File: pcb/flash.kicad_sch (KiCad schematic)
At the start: 7 parts, among them U4 W25Q128JVS

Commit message: Update project
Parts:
- added R29, R30, R31: 22, symbol Device:R_Small_US
- C23: value 1u -> 100n
- R15, R16, R18: value 22 -> 47k
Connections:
- net +3V3: now also R15.1, R16.1, R18.1
- net IO1: now also R29.1; no longer R15.1
- net IO2: now also R30.1; no longer R16.1
- net IO3: now also R31.1; no longer R18.1
- net ~{CS}: now also R15.2
- net at U4.2 (DO/IO_{1}): now also R16.2, R29.2; no longer R15.2
- net at R18.2: now also U4.3 (~{WP}/IO_{2}), R30.2; no longer U4.7 (~{HOLD}/~{RESET}/IO_{3})
- new net: R31.2, U4.7 (~{HOLD}/~{RESET}/IO_{3})
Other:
- note added: "close to MCU TODO: check this tho"
- note added: "or larger is OK"
- moved on the sheet: C23

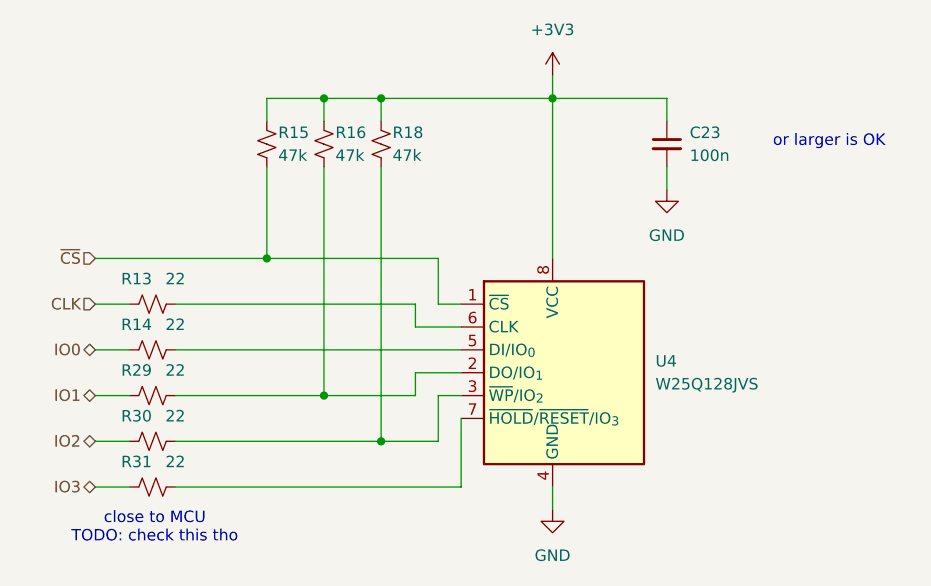
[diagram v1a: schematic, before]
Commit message: Adjust flash diagram to make room for pullups
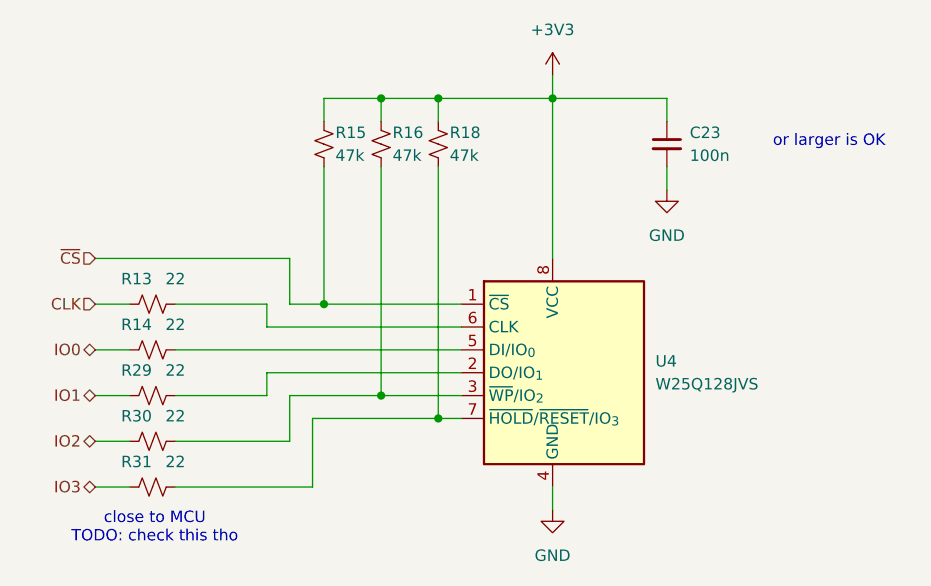
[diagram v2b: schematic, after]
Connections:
- net at R29.2, U4.2 (DO/IO_{1}): no longer R16.2
- net at R30.2, U4.3 (~{WP}/IO_{2}): now also R16.2; no longer R18.2
- net at R31.2, U4.7 (~{HOLD}/~{RESET}/IO_{3}): now also R18.2
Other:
- moved on the sheet: R15, R16, R18

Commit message: Start layout
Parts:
- C23: footprint (none) -> Capacitor_SMD:C_0603_1608Metric
- R20: renamed from R13; footprint (none) -> Resistor_SMD:R_0603_1608Metric
- R21: renamed from R14; footprint (none) -> Resistor_SMD:R_0603_1608Metric
- R22: renamed from R29; footprint (none) -> Resistor_SMD:R_0603_1608Metric
- R23: renamed from R30; footprint (none) -> Resistor_SMD:R_0603_1608Metric
- R24: renamed from R31; footprint (none) -> Resistor_SMD:R_0603_1608Metric
- R25: renamed from R15; footprint (none) -> Resistor_SMD:R_0603_1608Metric
- R26: renamed from R16; footprint (none) -> Resistor_SMD:R_0603_1608Metric
- R27: renamed from R18; footprint (none) -> Resistor_SMD:R_0603_1608Metric
- renumbered U4 to U5
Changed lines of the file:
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@@
 		(on_board yes)
 		(dnp no)
-		(property "Reference" "R29"
+		(property "Reference" "R22"
 			(at 55.372 75.946 90)
 			(effects
@@
 			)
 		)
-		(property "Footprint" ""
+		(property "Footprint" "Resistor_SMD:R_0603_1608Metric"
 			(at 57.15 78.74 0)
 			(effects
@@
 			(project "airbrake_mod"
 				(path "/1f4fd4ed-9886-4375-a5ac-dc32d5760936/676f83b0-0619-4d44-bbd6-46e3265a2238"
-					(reference "R29")
+					(reference "R22")
 					(unit 1)
 				)
@@
 		(dnp no)
 		(fields_autoplaced yes)
-		(property "Reference" "#PWR043"
+		(property "Reference" "#PWR054"
 			(at 114.3 62.23 0)
 			(effects
@@
 			(project ""
 				(path "/1f4fd4ed-9886-4375-a5ac-dc32d5760936/676f83b0-0619-4d44-bbd6-46e3265a2238"
-					(reference "#PWR043")
+					(reference "#PWR054")
 					(unit 1)
 				)
@@
 		(dnp no)
 		(fields_autoplaced yes)
-		(property "Reference" "#PWR036"
+		(property "Reference" "#PWR052"
 			(at 101.6 46.99 0)
 			(effects
@@
 			(project ""
 				(path "/1f4fd4ed-9886-4375-a5ac-dc32d5760936/676f83b0-0619-4d44-bbd6-46e3265a2238"
-					(reference "#PWR036")
+					(reference "#PWR052")
 					(unit 1)
 				)
@@
 		(on_board yes)
 		(dnp no)
-		(property "Reference" "R14"
+		(property "Reference" "R21"
 			(at 55.372 70.866 90)
 			(effects
@@
 			)
 		)
-		(property "Footprint" ""
+		(property "Footprint" "Resistor_SMD:R_0603_1608Metric"
 			(at 57.15 73.66 0)
 			(effects
@@
 			(project "airbrake_mod"
 				(path "/1f4fd4ed-9886-4375-a5ac-dc32d5760936/676f83b0-0619-4d44-bbd6-46e3265a2238"
-					(reference "R14")
+					(reference "R21")
 					(unit 1)
 				)
@@
 		(on_board yes)
 		(dnp no)
-		(property "Reference" "R30"
+		(property "Reference" "R23"
 			(at 55.372 81.026 90)
 			(effects
@@
 			)
 		)
-		(property "Footprint" ""
+		(property "Footprint" "Resistor_SMD:R_0603_1608Metric"
 			(at 57.15 83.82 0)
 			(effects
@@
 			(project "airbrake_mod"
 				(path "/1f4fd4ed-9886-4375-a5ac-dc32d5760936/676f83b0-0619-4d44-bbd6-46e3265a2238"
-					(reference "R30")
+					(reference "R23")
 					(unit 1)
 				)
@@
 		(on_board yes)
 		(dnp no)
-		(property "Reference" "R13"
+		(property "Reference" "R20"
 			(at 55.372 65.786 90)
 			(effects
@@
 			)
 		)
-		(property "Footprint" ""
+		(property "Footprint" "Resistor_SMD:R_0603_1608Metric"
 			(at 57.15 68.58 0)
 			(effects
@@
 			(project ""
 				(path "/1f4fd4ed-9886-4375-a5ac-dc32d5760936/676f83b0-0619-4d44-bbd6-46e3265a2238"
-					(reference "R13")
+					(reference "R20")
 					(unit 1)
 				)
@@
 		(dnp no)
 		(fields_autoplaced yes)
-		(property "Reference" "#PWR045"
+		(property "Reference" "#PWR053"
 			(at 101.6 97.79 0)
 			(effects
@@
 			(project "airbrake_mod"
 				(path "/1f4fd4ed-9886-4375-a5ac-dc32d5760936/676f83b0-0619-4d44-bbd6-46e3265a2238"
-					(reference "#PWR045")
+					(reference "#PWR053")
 					(unit 1)
 				)
@@
 		(on_board yes)
 		(dnp no)
-		(property "Reference" "R15"
+		(property "Reference" "R25"
 			(at 77.47 49.53 0)
 			(effects
@@
 			)
 		)
-		(property "Footprint" ""
+		(property "Footprint" "Resistor_SMD:R_0603_1608Metric"
 			(at 76.2 50.8 0)
 			(effects
@@
 			(project "airbrake_mod"
 				(path "/1f4fd4ed-9886-4375-a5ac-dc32d5760936/676f83b0-0619-4d44-bbd6-46e3265a2238"
-					(reference "R15")
+					(reference "R25")
 					(unit 1)
 				)
@@
 		(on_board yes)
 		(dnp no)
-		(property "Reference" "R18"
+		(property "Reference" "R27"
 			(at 90.17 49.53 0)
 			(effects
@@
 			)
 		)
-		(property "Footprint" ""
+		(property "Footprint" "Resistor_SMD:R_0603_1608Metric"
 			(at 88.9 50.8 0)
 			(effects
@@
 			(project "airbrake_mod"
 				(path "/1f4fd4ed-9886-4375-a5ac-dc32d5760936/676f83b0-0619-4d44-bbd6-46e3265a2238"
-					(reference "R18")
+					(reference "R27")
 					(unit 1)
 				)
@@
 		(dnp no)
 		(fields_autoplaced yes)
-		(property "Reference" "U4"
+		(property "Reference" "U5"
 			(at 113.03 74.9299 0)
 			(effects
@@
 			(project ""
 				(path "/1f4fd4ed-9886-4375-a5ac-dc32d5760936/676f83b0-0619-4d44-bbd6-46e3265a2238"
-					(reference "U4")
+					(reference "U5")
 					(unit 1)
 				)
@@
 		(on_board yes)
 		(dnp no)
-		(property "Reference" "R31"
+		(property "Reference" "R24"
 			(at 55.372 86.106 90)
 			(effects
@@
 			)
 		)
-		(property "Footprint" ""
+		(property "Footprint" "Resistor_SMD:R_0603_1608Metric"
 			(at 57.15 88.9 0)
 			(effects
@@
 			(project "airbrake_mod"
 				(path "/1f4fd4ed-9886-4375-a5ac-dc32d5760936/676f83b0-0619-4d44-bbd6-46e3265a2238"
-					(reference "R31")
+					(reference "R24")
 					(unit 1)
 				)
@@
 		(on_board yes)
 		(dnp no)
-		(property "Reference" "R16"
+		(property "Reference" "R26"
 			(at 83.82 49.53 0)
 			(effects
@@
 			)
 		)
-		(property "Footprint" ""
+		(property "Footprint" "Resistor_SMD:R_0603_1608Metric"
 			(at 82.55 50.8 0)
 			(effects
@@
 			(project "airbrake_mod"
 				(path "/1f4fd4ed-9886-4375-a5ac-dc32d5760936/676f83b0-0619-4d44-bbd6-46e3265a2238"
-					(reference "R16")
+					(reference "R26")
 					(unit 1)
 				)
@@
 			)
 		)
-		(property "Footprint" ""
+		(property "Footprint" "Capacitor_SMD:C_0603_1608Metric"
 			(at 114.3 50.8 0)
 			(effects

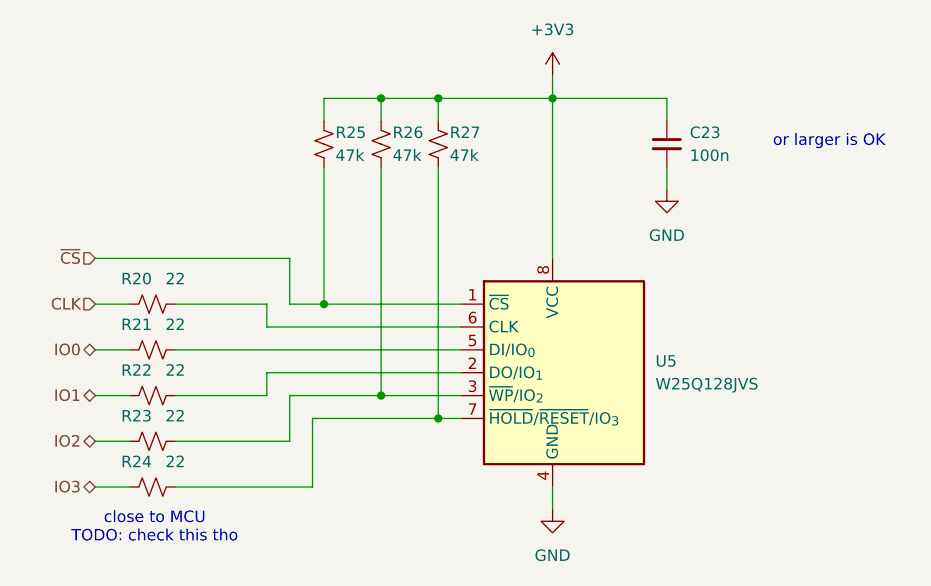
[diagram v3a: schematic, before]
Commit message: Layout MCU decoupling
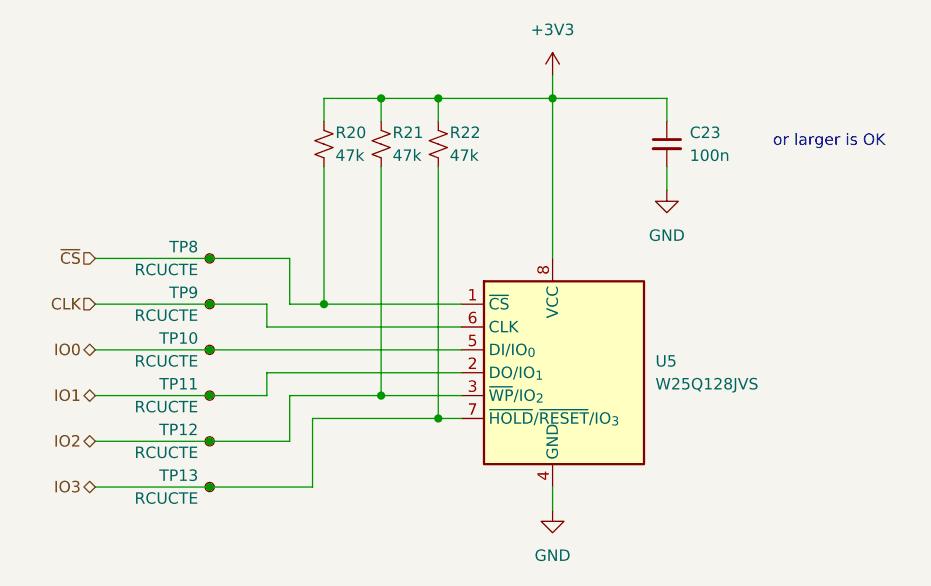
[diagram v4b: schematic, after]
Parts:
- removed R20, R21, R22, R23, R24: 22, Resistor_SMD:R_0603_1608Metric, symbol Device:R_Small_US
- added TP10, TP11, TP12, TP13, TP8, TP9: RCUCTE, TestPoint_KOASpeer:TestPoint_Chip_RCUCTE_0603, symbol Connector:TestPoint_Small
- renumbered R25 to R20, R26 to R21, R27 to R22
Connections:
- net CLK: now also U5.6 (CLK), TP9.1
- net IO0: now also U5.5 (DI/IO_{0}), TP10.1
- net IO1: now also U5.2 (DO/IO_{1}), TP11.1
- net IO2: now also R21.2, U5.3 (~{WP}/IO_{2}), TP12.1
- net IO3: now also R22.2, U5.7 (~{HOLD}/~{RESET}/IO_{3}), TP13.1
- net ~{CS}: now also TP8.1
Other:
- note removed: "close to MCU TODO: check this tho"

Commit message: Incorporate feedback servo with 4 pin molex and additional ADC channel
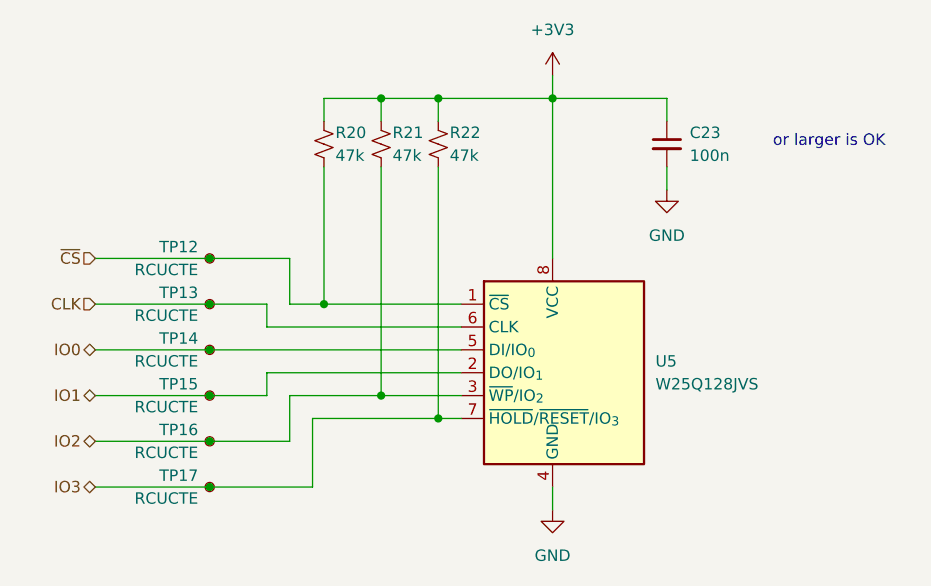
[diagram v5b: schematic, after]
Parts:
- renumbered TP8 to TP12, TP9 to TP13, TP10 to TP14, TP11 to TP15, TP12 to TP16, TP13 to TP17
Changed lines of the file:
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@@
 		(dnp no)
 		(fields_autoplaced yes)
-		(property "Reference" "TP10"
+		(property "Reference" "TP14"
 			(at 62.23 72.3899 0)
 			(effects
@@
 			(project "airbrake_mod"
 				(path "/1f4fd4ed-9886-4375-a5ac-dc32d5760936/676f83b0-0619-4d44-bbd6-46e3265a2238"
-					(reference "TP10")
+					(reference "TP14")
 					(unit 1)
 				)
@@
 		(dnp no)
 		(fields_autoplaced yes)
-		(property "Reference" "#PWR054"
+		(property "Reference" "#PWR058"
 			(at 114.3 62.23 0)
 			(effects
@@
 			(project ""
 				(path "/1f4fd4ed-9886-4375-a5ac-dc32d5760936/676f83b0-0619-4d44-bbd6-46e3265a2238"
-					(reference "#PWR054")
+					(reference "#PWR058")
 					(unit 1)
 				)
@@
 		(dnp no)
 		(fields_autoplaced yes)
-		(property "Reference" "TP8"
+		(property "Reference" "TP12"
 			(at 62.23 62.2299 0)
 			(effects
@@
 			(project ""
 				(path "/1f4fd4ed-9886-4375-a5ac-dc32d5760936/676f83b0-0619-4d44-bbd6-46e3265a2238"
-					(reference "TP8")
+					(reference "TP12")
 					(unit 1)
 				)
@@
 		(dnp no)
 		(fields_autoplaced yes)
-		(property "Reference" "#PWR052"
+		(property "Reference" "#PWR056"
 			(at 101.6 46.99 0)
 			(effects
@@
 			(project ""
 				(path "/1f4fd4ed-9886-4375-a5ac-dc32d5760936/676f83b0-0619-4d44-bbd6-46e3265a2238"
-					(reference "#PWR052")
+					(reference "#PWR056")
 					(unit 1)
 				)
@@
 		(dnp no)
 		(fields_autoplaced yes)
-		(property "Reference" "#PWR053"
+		(property "Reference" "#PWR057"
 			(at 101.6 97.79 0)
 			(effects
@@
 			(project "airbrake_mod"
 				(path "/1f4fd4ed-9886-4375-a5ac-dc32d5760936/676f83b0-0619-4d44-bbd6-46e3265a2238"
-					(reference "#PWR053")
+					(reference "#PWR057")
 					(unit 1)
 				)
@@
 		(dnp no)
 		(fields_autoplaced yes)
-		(property "Reference" "TP12"
+		(property "Reference" "TP16"
 			(at 62.23 82.5499 0)
 			(effects
@@
 			(project "airbrake_mod"
 				(path "/1f4fd4ed-9886-4375-a5ac-dc32d5760936/676f83b0-0619-4d44-bbd6-46e3265a2238"
-					(reference "TP12")
+					(reference "TP16")
 					(unit 1)
 				)
@@
 		(dnp no)
 		(fields_autoplaced yes)
-		(property "Reference" "TP13"
+		(property "Reference" "TP17"
 			(at 62.23 87.6299 0)
 			(effects
@@
 			(project "airbrake_mod"
 				(path "/1f4fd4ed-9886-4375-a5ac-dc32d5760936/676f83b0-0619-4d44-bbd6-46e3265a2238"
-					(reference "TP13")
+					(reference "TP17")
 					(unit 1)
 				)
@@
 		(dnp no)
 		(fields_autoplaced yes)
-		(property "Reference" "TP11"
+		(property "Reference" "TP15"
 			(at 62.23 77.4699 0)
 			(effects
@@
 			(project "airbrake_mod"
 				(path "/1f4fd4ed-9886-4375-a5ac-dc32d5760936/676f83b0-0619-4d44-bbd6-46e3265a2238"
-					(reference "TP11")
+					(reference "TP15")
 					(unit 1)
 				)
@@
 		(dnp no)
 		(fields_autoplaced yes)
-		(property "Reference" "TP9"
+		(property "Reference" "TP13"
 			(at 62.23 67.3099 0)
 			(effects
@@
 			(project "airbrake_mod"
 				(path "/1f4fd4ed-9886-4375-a5ac-dc32d5760936/676f83b0-0619-4d44-bbd6-46e3265a2238"
-					(reference "TP9")
-					(unit 1)
-				)
+					(reference "TP13")
+					(unit 1)
+				)

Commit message: Add buck enable switch
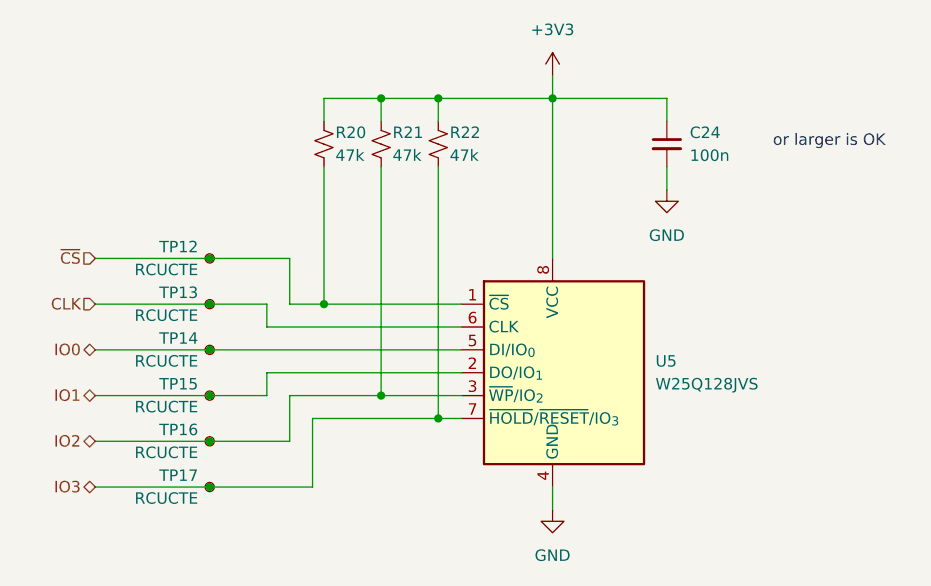
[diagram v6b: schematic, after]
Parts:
- renumbered C23 to C24
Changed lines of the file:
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@@
 		(dnp no)
 		(fields_autoplaced yes)
-		(property "Reference" "#PWR058"
+		(property "Reference" "#PWR059"
 			(at 114.3 62.23 0)
 			(effects
@@
 			(project ""
 				(path "/1f4fd4ed-9886-4375-a5ac-dc32d5760936/676f83b0-0619-4d44-bbd6-46e3265a2238"
-					(reference "#PWR058")
+					(reference "#PWR059")
 					(unit 1)
 				)
@@
 		(dnp no)
 		(fields_autoplaced yes)
-		(property "Reference" "#PWR056"
+		(property "Reference" "#PWR057"
 			(at 101.6 46.99 0)
 			(effects
@@
 			(project ""
 				(path "/1f4fd4ed-9886-4375-a5ac-dc32d5760936/676f83b0-0619-4d44-bbd6-46e3265a2238"
-					(reference "#PWR056")
+					(reference "#PWR057")
 					(unit 1)
 				)
@@
 		(dnp no)
 		(fields_autoplaced yes)
-		(property "Reference" "#PWR057"
+		(property "Reference" "#PWR058"
 			(at 101.6 97.79 0)
 			(effects
@@
 			(project "airbrake_mod"
 				(path "/1f4fd4ed-9886-4375-a5ac-dc32d5760936/676f83b0-0619-4d44-bbd6-46e3265a2238"
-					(reference "#PWR057")
+					(reference "#PWR058")
 					(unit 1)
 				)
@@
 		(dnp no)
 		(fields_autoplaced yes)
-		(property "Reference" "C23"
+		(property "Reference" "C24"
 			(at 116.84 49.5362 0)
 			(effects
@@
 			(project ""
 				(path "/1f4fd4ed-9886-4375-a5ac-dc32d5760936/676f83b0-0619-4d44-bbd6-46e3265a2238"
-					(reference "C23")
-					(unit 1)
-				)
+					(reference "C24")
+					(unit 1)
+				)

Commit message: Add CUR schematic sheet title block
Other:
- company: (none) -> Clarkson University Rocketry Team
- title: (none) -> Air Brakes Module
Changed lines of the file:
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@@
 	(generator_version "9.0")
 	(paper "A4")
+	(title_block
+		(title "Air Brakes Module")
+		(date "2025-11-23")
+		(company "Clarkson University Rocketry Team")
+	)
 	(text "or larger is OK"
 		(exclude_from_sim no)
